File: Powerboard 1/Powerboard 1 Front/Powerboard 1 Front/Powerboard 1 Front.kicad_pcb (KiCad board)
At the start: 2 copper layers, 40 x 128.5 mm, 0 parts

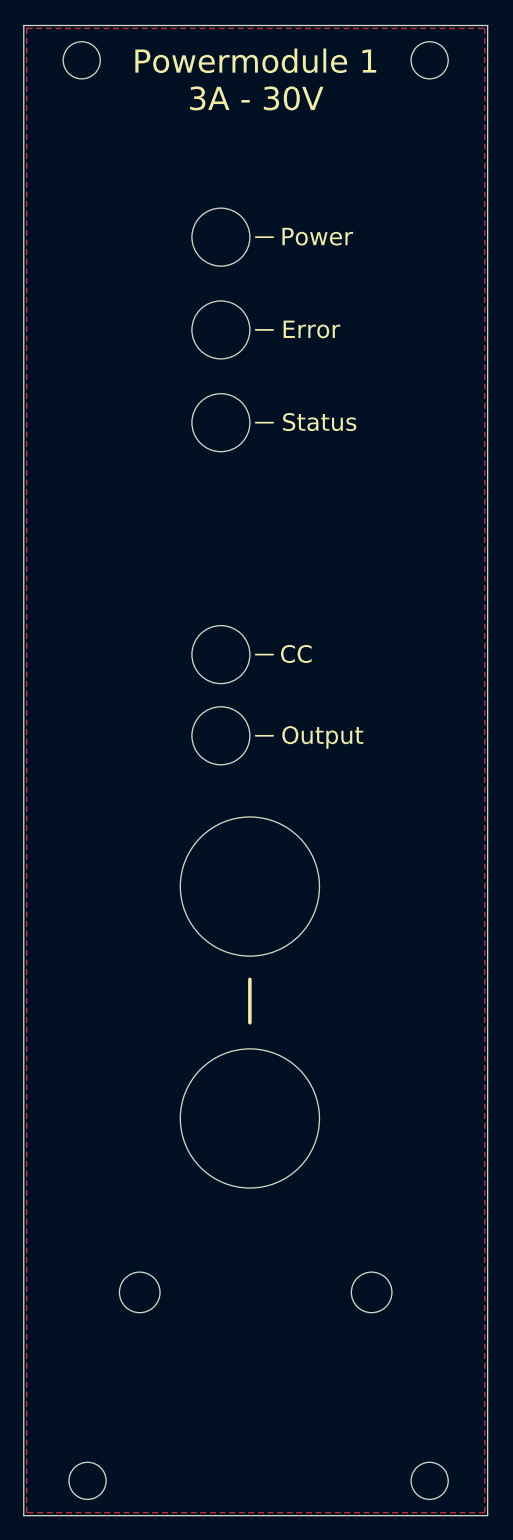
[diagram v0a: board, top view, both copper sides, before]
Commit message: updated powerboard front to remove copper
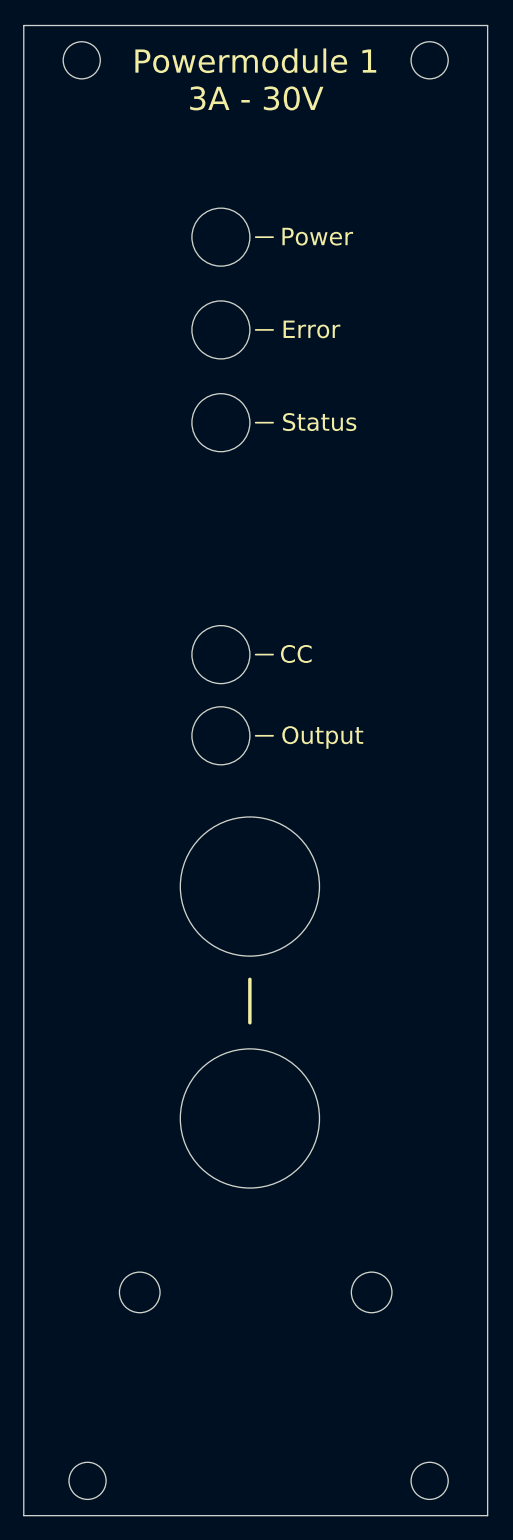
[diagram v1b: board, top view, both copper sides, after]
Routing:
- removed copper zone on F.Cu, net (none)
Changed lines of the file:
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@@
     (effects (font (size 1.5 1.5) (thickness 0.15)))
   )
-  (zone (net 0) (net_name "") (layer "F.Cu") (hatch edge 0.508)
-    (connect_pads (clearance 0.508))
-    (min_thickness 0.254) (filled_areas_thickness no)
-    (fill yes (thermal_gap 0.508) (thermal_bridge_width 0.508))
-    (polygon
-      (pts
-        (xy 59.75 148.25)
-        (xy 20.25 148.25)
-        (xy 20.25 20.25)
-        (xy 59.75 20.25)
-      )
-    )
-  )
 )

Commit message: Rev 3 Pcb's
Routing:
- added copper zone on F.Cu, net (none)
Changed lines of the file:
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@@
       (drillshape 0)
       (scaleselection 1)
-      (outputdirectory "")
+      (outputdirectory "Gerber/")
     )
   )
@@
     (effects (font (size 1.5 1.5) (thickness 0.15)))
   )
+  (zone (net 0) (net_name "") (layer "F.Cu") (hatch edge 0.508)
+    (connect_pads (clearance 0.508))
+    (min_thickness 0.254) (filled_areas_thickness no)
+    (fill yes (thermal_gap 0.508) (thermal_bridge_width 0.508) (smoothing fillet) (radius 1))
+    (polygon
+      (pts
+        (xy 60.2 148.6)
+        (xy 20 148.6)
+        (xy 20 19.8)
+        (xy 60.2 19.8)
+      )
+    )
+  )
 )
